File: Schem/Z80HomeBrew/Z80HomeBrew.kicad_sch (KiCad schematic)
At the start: 0 parts

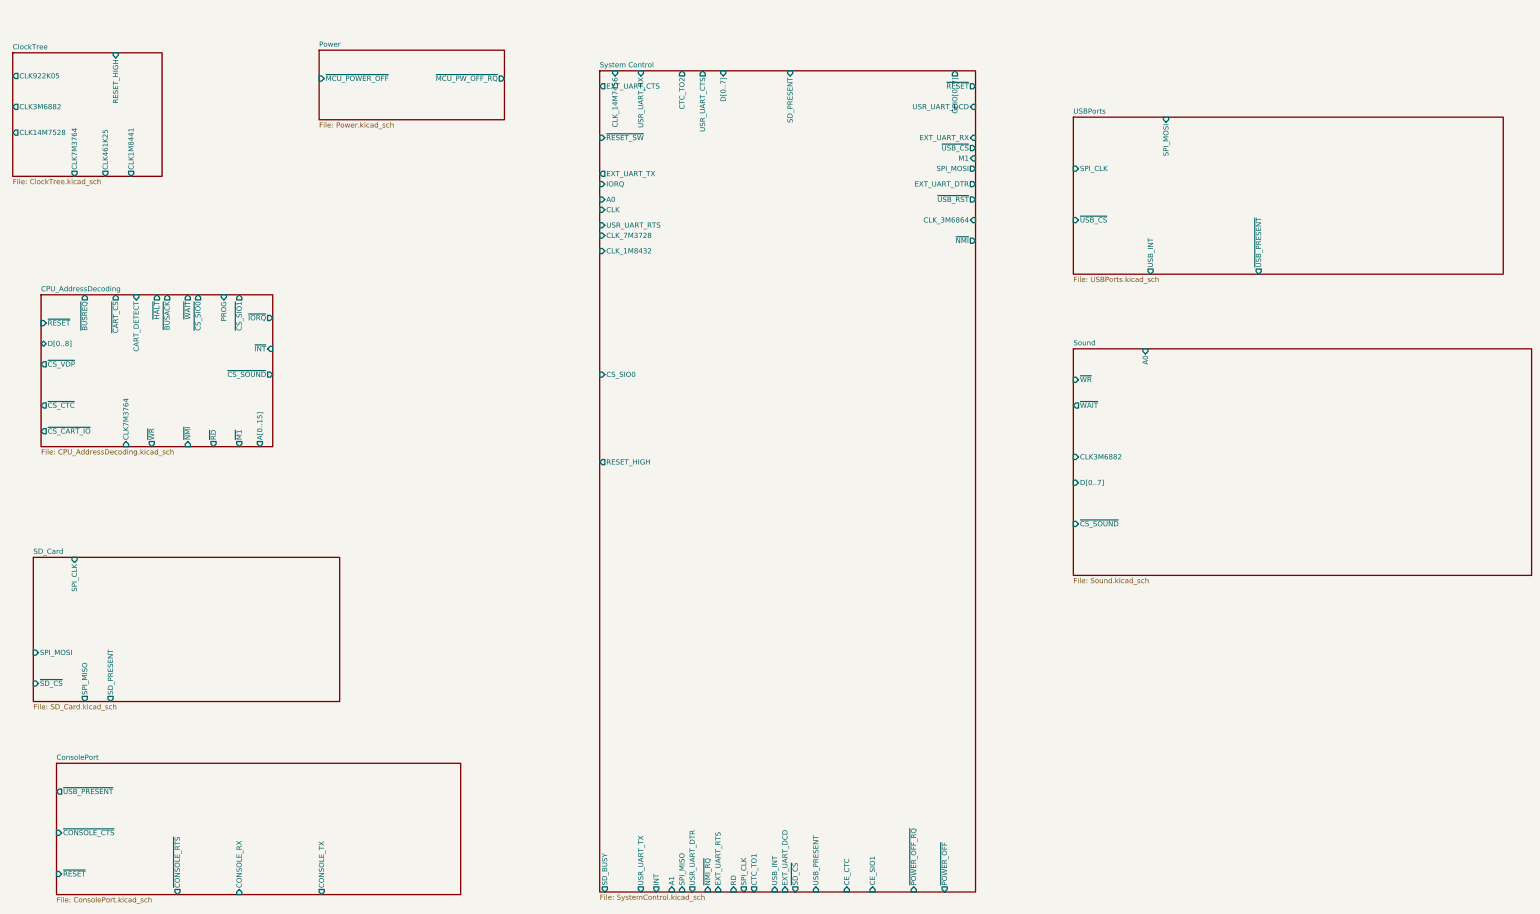
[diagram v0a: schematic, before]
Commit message: Video block added. fixed some issues with parts...
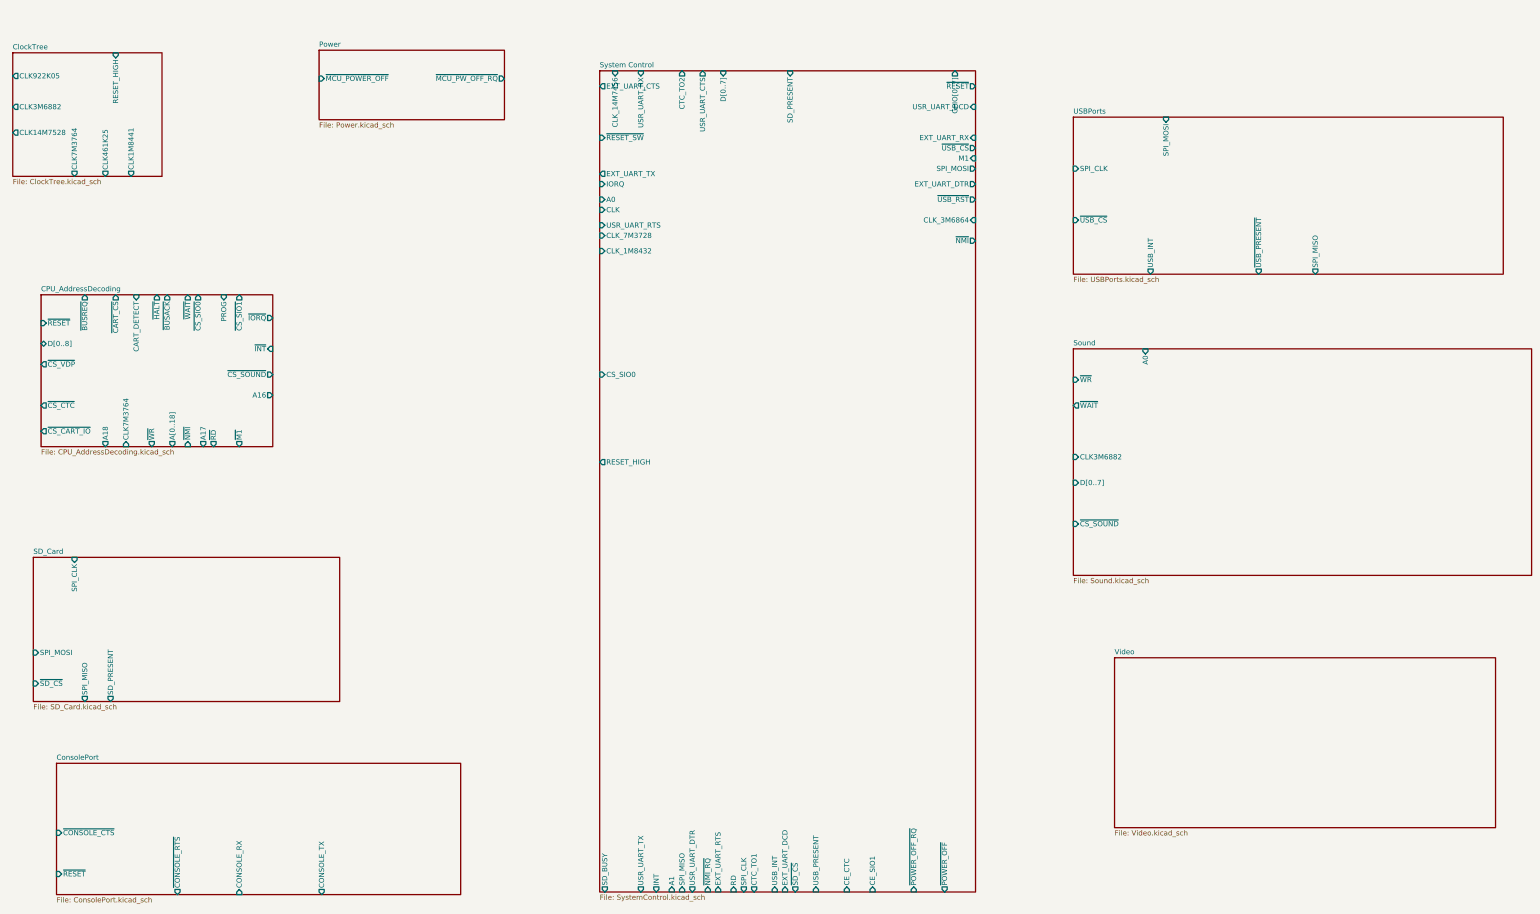
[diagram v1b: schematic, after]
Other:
- added sheet Video (Video.kicad_sch)
- sheet CPU_AddressDecoding ports: added A16, A17, A18, A[0..18]; removed A[0..15]
- sheet ConsolePort ports: added none; removed ~{USB_PRESENT}
- sheet USBPorts ports: added SPI_MISO; removed none
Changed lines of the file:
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@@
+			)
+		)
+		(pin "SPI_MISO" output
+			(at 354.33 84.455 270)
+			(effects
+				(font
+					(size 1.27 1.27)
+				)
+				(justify left)
 			)
 		)
@@
 	)
 	(sheet
+		(at 304.8 179.07)
+		(size 93.98 41.91)
+		(exclude_from_sim no)
+		(in_bom yes)
+		(on_board yes)
+		(dnp no)
+		(fields_autoplaced yes)
+		(stroke
+			(width 0.1524)
+			(type solid)
+		)
+		(fill
+			(color 0 0 0 0.0000)
+		)
+		(property "Sheetname" "Video"
+			(at 304.8 178.3584 0)
+			(effects
+				(font
+					(size 1.27 1.27)
+				)
+				(justify left bottom)
+			)
+		)
+		(property "Sheetfile" "Video.kicad_sch"
+			(at 304.8 221.5646 0)
+			(effects
+				(font
+					(size 1.27 1.27)
+				)
+				(justify left top)
+			)
+		)
+		(instances
+			(project "Z80HomeBrew"
+				(path "/5593e793-d133-45d0-a91e-72805049e474"
+					(page "10")
+				)
+			)
+		)
+	)
+	(sheet
 		(at 40.005 89.535)
 		(size 57.15 37.465)
@@
 			)
 		)
-		(pin "A[0..15]" output
-			(at 93.98 127 270)
-			(effects
-				(font
-					(size 1.27 1.27)
-				)
-				(justify left)
-			)
-		)
 		(pin "~{CS_SOUND}" output
 			(at 97.155 109.22 0)
@@
 				)
 				(justify right)
+			)
+		)
+		(pin "A[0..18]" output
+			(at 72.39 127 270)
+			(effects
+				(font
+					(size 1.27 1.27)
+				)
+				(justify left)
+			)
+		)
+		(pin "A17" output
+			(at 80.01 127 270)
+			(effects
+				(font
+					(size 1.27 1.27)
+				)
+				(justify left)
+			)
+		)
+		(pin "A16" output
+			(at 97.155 114.3 0)
+			(effects
+				(font
+					(size 1.27 1.27)
+				)
+				(justify right)
+			)
+		)
+		(pin "A18" output
+			(at 55.88 127 270)
+			(effects
+				(font
+					(size 1.27 1.27)
+				)
+				(justify left)
 			)
 		)
@@
 			)
 		)
-		(pin "~{USB_PRESENT}" output
-			(at 43.815 212.09 180)
-			(effects
-				(font
-					(size 1.27 1.27)
-				)
-				(justify left)
-			)
-		)

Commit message: Completed schematics
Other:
- added sheet UserPorts (UserPorts.kicad_sch)
- sheet CPU_AddressDecoding ports: added A[0..15], D[0..7], EXP_IEI, IEI, ~{INT_VDP}, ~{MREQ}; removed A16, A17, A18, A[0..18], D[0..8]
- sheet ClockTree ports: added none; removed CLK461K25, CLK922K05
- sheet ConsolePort ports: added CONSOLE_CTS, CONSOLE_DTR, CONSOLE_RTS; removed ~{CONSOLE_CTS}, ~{CONSOLE_RTS}
- sheet System Control ports: added IEO, ~{INT}, ~{USB_PRESENT}; removed CLK, EXT_UART_DTR, INT, SD_BUSY, USB_PRESENT, USR_UART_DCD, USR_UART_DTR, ~{NMI_RQ}, ~{RESET_SW}, ~{USB_RST}
- sheet Video ports: added A0, A1, D[0..7], ~{CS_VDP}, ~{INT}, ~{NMI}, ~{RD}, ~{RESET}, ~{WR}; removed none

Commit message: Finally found a name "Zephyr-80" for the brew and committing the first pbc
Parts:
- added H1, H2, H3, H4, H5, H6: MountingHole_Pad, MountingHole:MountingHole_3.2mm_M3_Pad, symbol Mechanical:MountingHole_Pad
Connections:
- new net GND: H1.1, H2.1, H3.1, H4.1, H5.1, H6.1
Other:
- sheet Sound ports: added A1; removed none

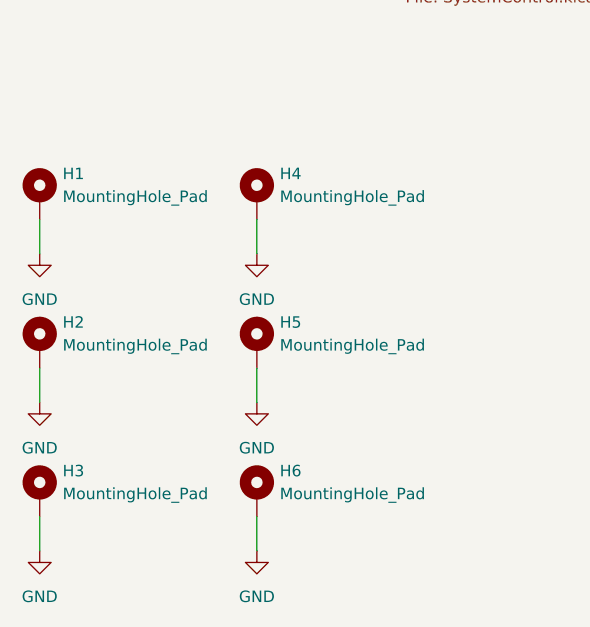
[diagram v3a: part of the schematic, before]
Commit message: Added pBITzBackplane and MezzanineConnector
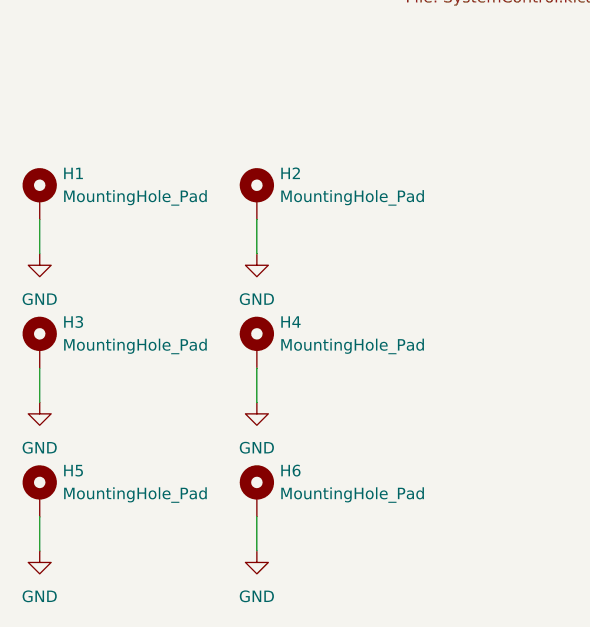
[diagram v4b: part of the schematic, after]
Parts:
- renumbered H4 to H2, H2 to H3, H5 to H4, H3 to H5
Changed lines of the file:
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@@
 		(dnp no)
 		(fields_autoplaced yes)
-		(property "Reference" "#PWR0156"
+		(property "Reference" "#PWR05"
 			(at 34.29 220.98 0)
 			(effects
@@
 			(project "Z80HomeBrew"
 				(path "/5593e793-d133-45d0-a91e-72805049e474"
-					(reference "#PWR0156")
+					(reference "#PWR05")
 					(unit 1)
 				)
@@
 		(dnp no)
 		(fields_autoplaced yes)
-		(property "Reference" "#PWR0155"
+		(property "Reference" "#PWR03"
 			(at 34.29 204.47 0)
 			(effects
@@
 			(project "Z80HomeBrew"
 				(path "/5593e793-d133-45d0-a91e-72805049e474"
-					(reference "#PWR0155")
+					(reference "#PWR03")
 					(unit 1)
 				)
@@
 		(dnp no)
 		(fields_autoplaced yes)
-		(property "Reference" "H2"
+		(property "Reference" "H3"
 			(at 36.83 189.2299 0)
 			(effects
@@
 			)
 		)
-		(pin "1"
-		)
-		(instances
-			(project "Z80HomeBrew"
-				(path "/5593e793-d133-45d0-a91e-72805049e474"
-					(reference "H2")
+		(property "KLC_S4.2_3V3OUT" ""
+			(at 34.29 191.77 0)
+			(effects
+				(font
+					(size 1.27 1.27)
+				)
+				(hide yes)
+			)
+		)
+		(property "KLC_S4.2_VCC" ""
+			(at 34.29 191.77 0)
+			(effects
+				(font
+					(size 1.27 1.27)
+				)
+				(hide yes)
+			)
+		)
+		(pin "1"
+		)
+		(instances
+			(project "Z80HomeBrew"
+				(path "/5593e793-d133-45d0-a91e-72805049e474"
+					(reference "H3")
 					(unit 1)
 				)
@@
 		(dnp no)
 		(fields_autoplaced yes)
-		(property "Reference" "#PWR0157"
+		(property "Reference" "#PWR02"
 			(at 58.42 187.96 0)
 			(effects
@@
 			(project "Z80HomeBrew"
 				(path "/5593e793-d133-45d0-a91e-72805049e474"
-					(reference "#PWR0157")
+					(reference "#PWR02")
 					(unit 1)
 				)
@@
 		(dnp no)
 		(fields_autoplaced yes)
-		(property "Reference" "H3"
+		(property "Reference" "H5"
 			(at 36.83 205.7399 0)
 			(effects
@@
 			)
 		)
-		(pin "1"
-		)
-		(instances
-			(project "Z80HomeBrew"
-				(path "/5593e793-d133-45d0-a91e-72805049e474"
-					(reference "H3")
+		(property "KLC_S4.2_3V3OUT" ""
+			(at 34.29 208.28 0)
+			(effects
+				(font
+					(size 1.27 1.27)
+				)
+				(hide yes)
+			)
+		)
+		(property "KLC_S4.2_VCC" ""
+			(at 34.29 208.28 0)
+			(effects
+				(font
+					(size 1.27 1.27)
+				)
+				(hide yes)
+			)
+		)
+		(pin "1"
+		)
+		(instances
+			(project "Z80HomeBrew"
+				(path "/5593e793-d133-45d0-a91e-72805049e474"
+					(reference "H5")
 					(unit 1)
 				)
@@
 		(dnp no)
 		(fields_autoplaced yes)
-		(property "Reference" "#PWR0159"
+		(property "Reference" "#PWR06"
 			(at 58.42 220.98 0)
 			(effects
@@
 			(project "Z80HomeBrew"
 				(path "/5593e793-d133-45d0-a91e-72805049e474"
-					(reference "#PWR0159")
+					(reference "#PWR06")
 					(unit 1)
 				)
@@
 		(dnp no)
 		(fields_autoplaced yes)
-		(property "Reference" "#PWR0158"
+		(property "Reference" "#PWR04"
 			(at 58.42 204.47 0)
 			(effects
@@
 			(project "Z80HomeBrew"
 				(path "/5593e793-d133-45d0-a91e-72805049e474"
-					(reference "#PWR0158")
+					(reference "#PWR04")
 					(unit 1)
 				)
@@
 			)
 		)
+		(property "KLC_S4.2_3V3OUT" ""
+			(at 58.42 208.28 0)
+			(effects
+				(font
+					(size 1.27 1.27)
+				)
+				(hide yes)
+			)
+		)
+		(property "KLC_S4.2_VCC" ""
+			(at 58.42 208.28 0)
+			(effects
+				(font
+					(size 1.27 1.27)
+				)
+				(hide yes)
+			)
+		)
 		(pin "1"
 		)
@@
 			)
 		)
+		(property "KLC_S4.2_3V3OUT" ""
+			(at 34.29 175.26 0)
+			(effects
+				(font
+					(size 1.27 1.27)
+				)
+				(hide yes)
+			)
+		)
+		(property "KLC_S4.2_VCC" ""
+			(at 34.29 175.26 0)
+			(effects
+				(font
+					(size 1.27 1.27)
+				)
+				(hide yes)
+			)
+		)
 		(pin "1"
 		)
@@
 		(dnp no)
 		(fields_autoplaced yes)
-		(property "Reference" "H5"
+		(property "Reference" "H4"
 			(at 60.96 189.2299 0)
 			(effects
@@
 			)
 		)
-		(pin "1"
-		)
-		(instances
-			(project "Z80HomeBrew"
-				(path "/5593e793-d133-45d0-a91e-72805049e474"
-					(reference "H5")
+		(property "KLC_S4.2_3V3OUT" ""
+			(at 58.42 191.77 0)
+			(effects
+				(font
+					(size 1.27 1.27)
+				)
+				(hide yes)
+			)
+		)
+		(property "KLC_S4.2_VCC" ""
+			(at 58.42 191.77 0)
+			(effects
+				(font
+					(size 1.27 1.27)
+				)
+				(hide yes)
+			)
+		)
+		(pin "1"
+		)
+		(instances
+			(project "Z80HomeBrew"
+				(path "/5593e793-d133-45d0-a91e-72805049e474"
+					(reference "H4")
 					(unit 1)
 				)
@@
 		(dnp no)
 		(fields_autoplaced yes)
-		(property "Reference" "H4"
+		(property "Reference" "H2"
 			(at 60.96 172.7199 0)
 			(effects
@@
 			)
 		)
-		(pin "1"
-		)
-		(instances
-			(project "Z80HomeBrew"
-				(path "/5593e793-d133-45d0-a91e-72805049e474"
-					(reference "H4")
+		(property "KLC_S4.2_3V3OUT" ""
+			(at 58.42 175.26 0)
+			(effects
+				(font
+					(size 1.27 1.27)
+				)
+				(hide yes)
+			)
+		)
+		(property "KLC_S4.2_VCC" ""
+			(at 58.42 175.26 0)
+			(effects
+				(font
+					(size 1.27 1.27)
+				)
+				(hide yes)
+			)
+		)
+		(pin "1"
+		)
+		(instances
+			(project "Z80HomeBrew"
+				(path "/5593e793-d133-45d0-a91e-72805049e474"
+					(reference "H2")
 					(unit 1)
 				)
@@
 		(dnp no)
 		(fields_autoplaced yes)
-		(property "Reference" "#PWR0148"
+		(property "Reference" "#PWR01"
 			(at 34.29 187.96 0)
 			(effects
@@
 			(project ""
 				(path "/5593e793-d133-45d0-a91e-72805049e474"
-					(reference "#PWR0148")
-					(unit 1)
-				)
+					(reference "#PWR01")
+					(unit 1)
+				)
